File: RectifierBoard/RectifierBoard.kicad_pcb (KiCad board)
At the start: 2 copper layers, 100 x 100 mm, 23 parts, among them J1 MKDS 1,5/2-7,62, J2 MKDS 5/ 4-7,62, J3 B+PI, J4 B+ Preamp

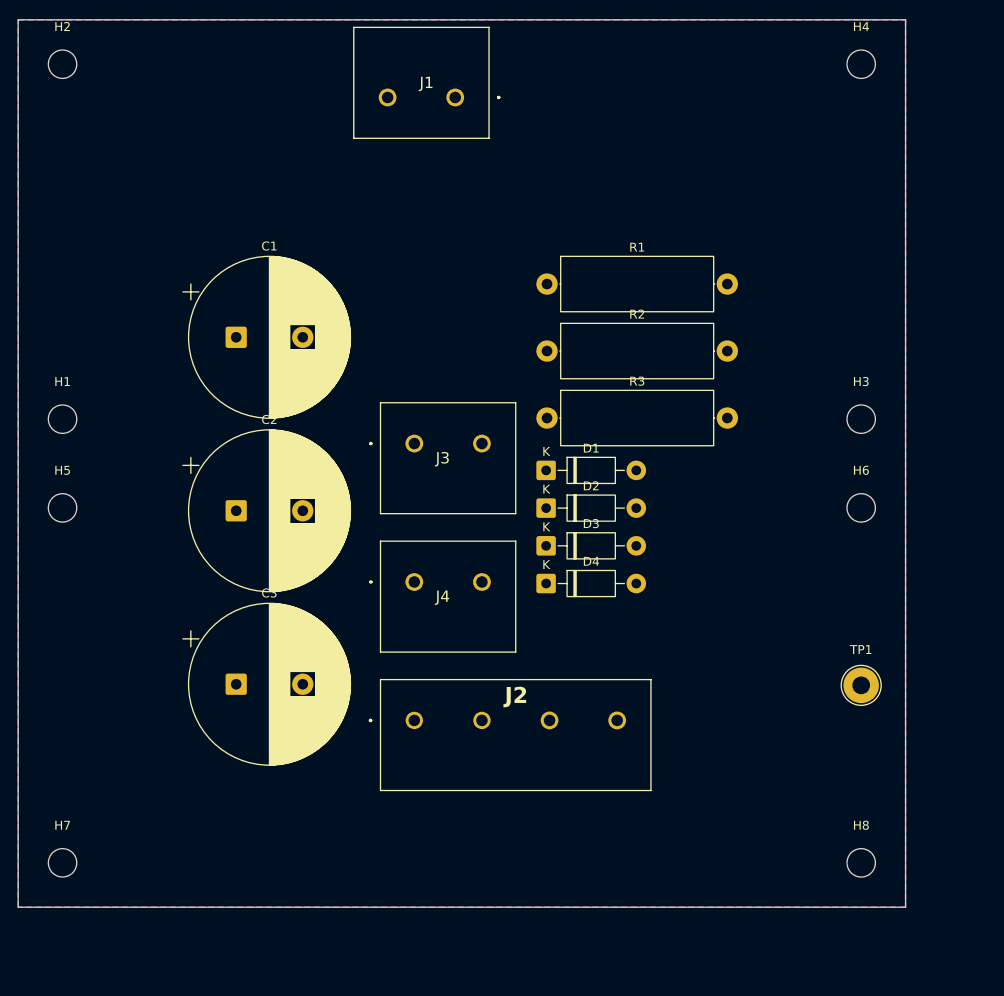
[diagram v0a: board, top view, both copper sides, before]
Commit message: First cut at PCB layout
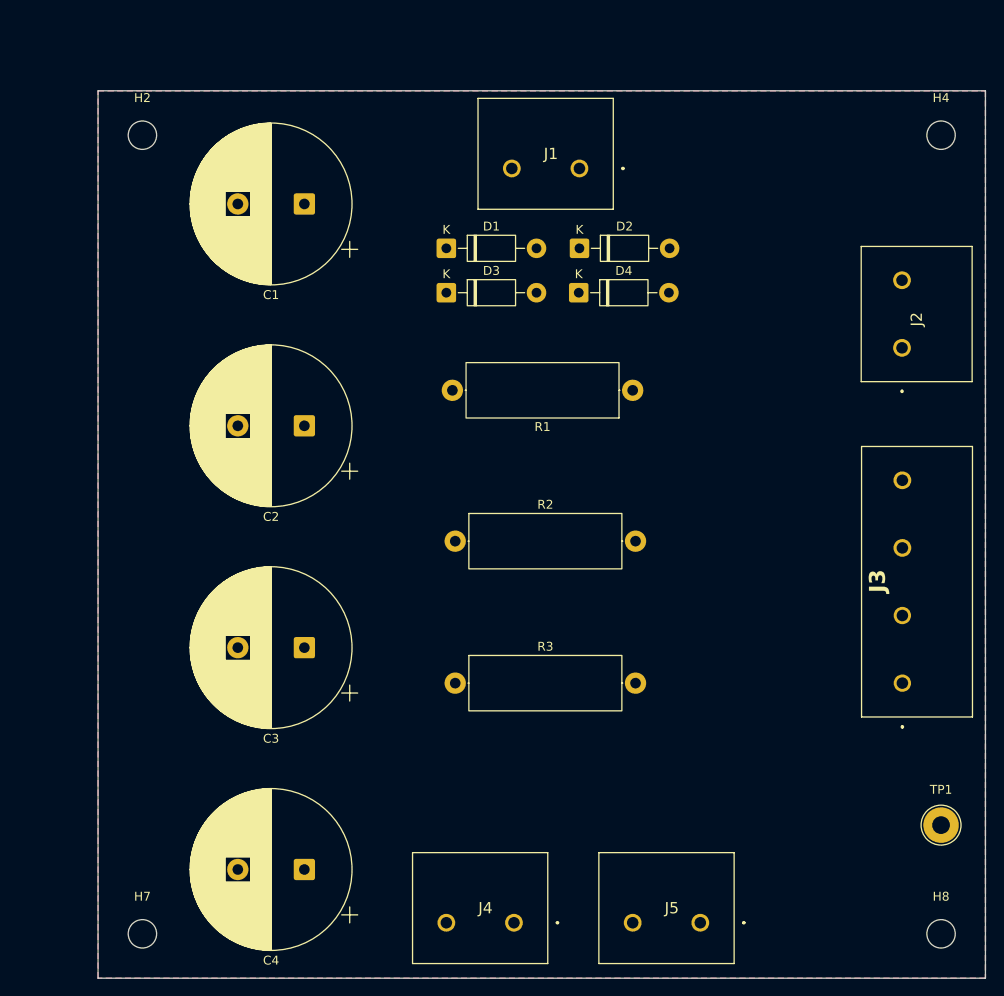
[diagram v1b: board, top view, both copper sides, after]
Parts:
- removed H1, H3, H5, H6: M3, MountingHole:MountingHole_3.2mm_M3
- added C3: 47µF, Capacitor_THT:CP_Radial_D18.0mm_P7.50mm, F.Cu at (123.0, 88.0)
- added J2: Standby, TerminalBlock_508:MKDS 5_2-7,62, F.Cu at (190.3, 54.2)
- J3: renamed from J2; value MKDS 5/ 4-7,62 -> L1 B+
- moved J3 55.2 mm to (190.4, 92.0), turned to 90 degrees
- moved J4 55.2 mm to (146.6, 119.0), turned to 180 degrees
- moved J5 50.1 mm to (167.6, 119.0), turned to 180 degrees
- moved D4 33.0 mm to (153.9, 48.0)
- moved R3 31.6 mm to (140.0, 92.0)
- moved D3 30.7 mm to (139.0, 48.0)
- moved D2 29.5 mm to (154.0, 43.0)
- moved D1 27.4 mm to (139.0, 43.0)
- moved R2 23.8 mm to (140.0, 76.0)
- moved C4 22.2 mm to (123.0, 113.0), turned to 180 degrees
- moved TP1 18.1 mm to (194.8, 108.0)
- moved C1 16.9 mm to (123.0, 38.0), turned to 180 degrees
- moved J1 16.1 mm to (154.0, 34.0)
- moved R1 15.4 mm to (160.0, 59.0), turned to 180 degrees
- moved C2 12.3 mm to (123.0, 63.0), turned to 180 degrees
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- renumbered C3 to C4, J3 to J4, J4 to J5
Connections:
- C2 pad 1: Net-(J2-Pin_3) -> Net-(J3-Pin_1)
- J3 pad 1: Net-(D1-K) -> Net-(J3-Pin_1)
- J3 pad 2: Net-(D1-K) -> Net-(J3-Pin_1)
- J3 pad 3: Net-(J2-Pin_3) -> Net-(J2-Pin_2)
- J3 pad 4: Net-(J2-Pin_3) -> Net-(J2-Pin_2)
- R2 pad 1: Net-(J2-Pin_3) -> Net-(J3-Pin_1)
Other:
- board text added: "Rectifier Board Andrew Fischer 14062026"
- board text removed: "MaxPlate 100x100 Andrew Fischer 21012022"

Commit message: Layout  - CORRECT GROUND ISSUE NEXT !!!!
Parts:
- J3: value L1 B+ -> B+ L1
- moved TP1 90.1 mm to (105.0, 100.0)
- moved J5 31.5 mm to (193.5, 101.0), turned to -90 degrees
- moved R2 20.4 mm to (160.0, 80.0), turned to 180 degrees
- moved D4 6.45 mm to (158.0, 53.0)
- moved R1 6.00 mm to (160.0, 65.0)
- moved D3 5.83 mm to (136.0, 53.0)
- moved J3 5.00 mm to (190.4, 87.0)
- moved J2 4.22 mm to (190.3, 50.0)
- moved D2 4.00 mm to (158.0, 43.0)
- moved R3 4.00 mm to (140.0, 96.0)
- moved D1 3.00 mm to (136.0, 43.0)
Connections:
- net Net-(D1-A) renamed /HT_AC_B
- net Net-(D3-A) renamed /HT_AC_A
- net Net-(J3-Pin_1) renamed /B+_L1_OUT
- net Net-(J4-Pin_1) renamed /B+_PI
- net Net-(J5-Pin_1) renamed /B+_PREAMP
- C1 pad 1: Net-(D1-K) -> /B+_PRE_STBY
- D1 pad 1: Net-(D1-K) -> /B+_PRE_STBY
- D3 pad 1: Net-(D1-K) -> /B+_PRE_STBY
- J2 pad 1: Net-(D1-K) -> /B+_STBY_OUT
- J2 pad 2: Net-(J2-Pin_2) -> /B+_PRE_STBY
- J3 pad 3: Net-(J2-Pin_2) -> /B+_STBY_OUT
- J3 pad 4: Net-(J2-Pin_2) -> /B+_STBY_OUT
- R1 pad 1: Net-(D1-K) -> /B+_PRE_STBY
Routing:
- net GND: track 0.00 -> 182.1 mm
- net /B+_PRE_STBY: track 0.00 -> 93.8 mm
- net /B+_L1_OUT: track 0.00 -> 82.3 mm
- net /B+_PREAMP: track 0.00 -> 79.6 mm
- net /B+_PI: track 0.00 -> 66.0 mm
- net /HT_AC_A: track 0.00 -> 33.4 mm
- net /B+_STBY_OUT: track 0.00 -> 21.8 mm
- net /HT_AC_B: track 0.00 -> 20.9 mm
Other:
- board text added: "+"
- board text added: "B+"
- board text added: "B+ PI"
- board text added: "B+ PRE"
- board text added: "BLEEDER DO NOT OMIT"
- board text added: "L1"

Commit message: Getting closer
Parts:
- J5: value B+ Preamp -> GND
- moved J5 49.8 mm to (146.0, 116.0), turned to 0 degrees
- moved J4 45.3 mm to (190.3, 107.2), turned to 90 degrees
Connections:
- J4 pad 1: /B+_PI -> /B+_PREAMP
- J4 pad 2: GND -> /B+_PI
- J5 pad 1: /B+_PREAMP -> GND
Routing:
- net /B+_PI: track 66.0 -> 103.5 mm
- net GND: track 182.1 -> 201.6 mm
- net /B+_PREAMP: track 79.6 -> 79.0 mm
- removed copper zone on B.Cu, net GND
- removed copper zone on F.Cu, net GND
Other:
- board text removed: "+"
